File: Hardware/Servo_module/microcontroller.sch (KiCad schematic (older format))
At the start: 22 parts, among them K1 CONN_3, K2 CONN_3, K3 CONN_3, K4 CONN_3, K5 CONN_3, K6 CONN_3, K7 CONN_3, K9 CONN_3, P1 CONN_4_JST, SW1 SW_PUSH

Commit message: [HARDWARE][SERVO_MODULE] Schematic
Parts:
- added D10, D11, D4, D5, D6, D7, D8, D9: LED, ~, symbol LED
- added R10, R11, R12, R13, R6, R7, R8, R9: 220, ~, symbol R
- gave numbers to parts that had none: 3
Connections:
- net +3.3V: now also U?.1 (VBAT)
- net GND: now also D10.2 (K), D11.2 (K), D4.2 (K), D5.2 (K), D6.2 (K), D7.2 (K), D8.2 (K), D9.2 (K)
- net NRST: now also U?.7 (NRST)
- net at U?.25 (PB12): now also R6.1
- net at U?.26 (PB13): now also R7.1
- net at U?.27 (PB14): now also R8.1
- net at U?.28 (PB15): now also R9.1
- net at U?.40 (PB4): now also R10.1
- net at U?.41 (PB5): now also R11.1
- net at U?.42 (PB6): now also R12.1
- net at U?.43 (PB7): now also R13.1
- new net: D4.1 (A), R6.2
- new net: D5.1 (A), R7.2
- new net: D6.1 (A), R8.2
- new net: D7.1 (A), R9.2
- new net: D8.1 (A), R10.2
- new net: D9.1 (A), R11.2
- new net: D10.1 (A), R12.2
- new net: D11.1 (A), R13.2
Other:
- note added: "TEST_LED"

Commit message: [HARDWARE][SERVO_MODULE] Schematic
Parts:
- C7, C8: value C -> 20p
- gave numbers to parts that had none: 1
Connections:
- net USART_PROG_RX: now also U1.31 (PA10)
- net USART_PROG_TX: now also U1.30 (PA9)

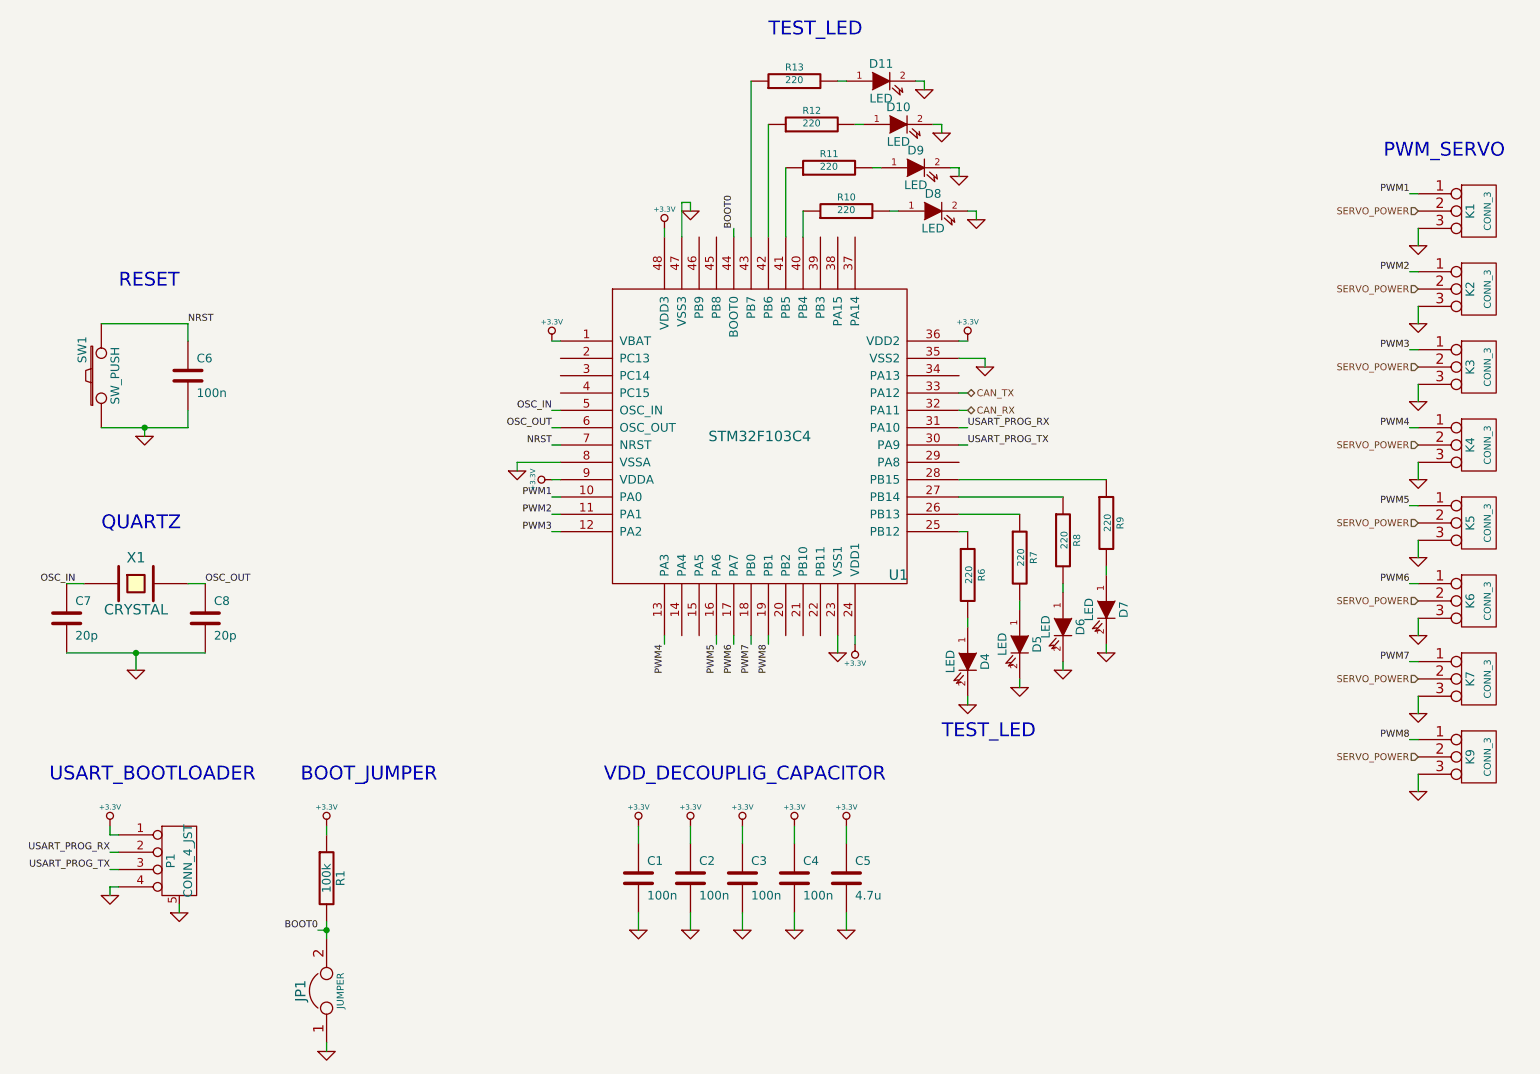
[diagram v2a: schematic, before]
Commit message: [HARDWARE][SERVO_MODULE] Update schemating & routing
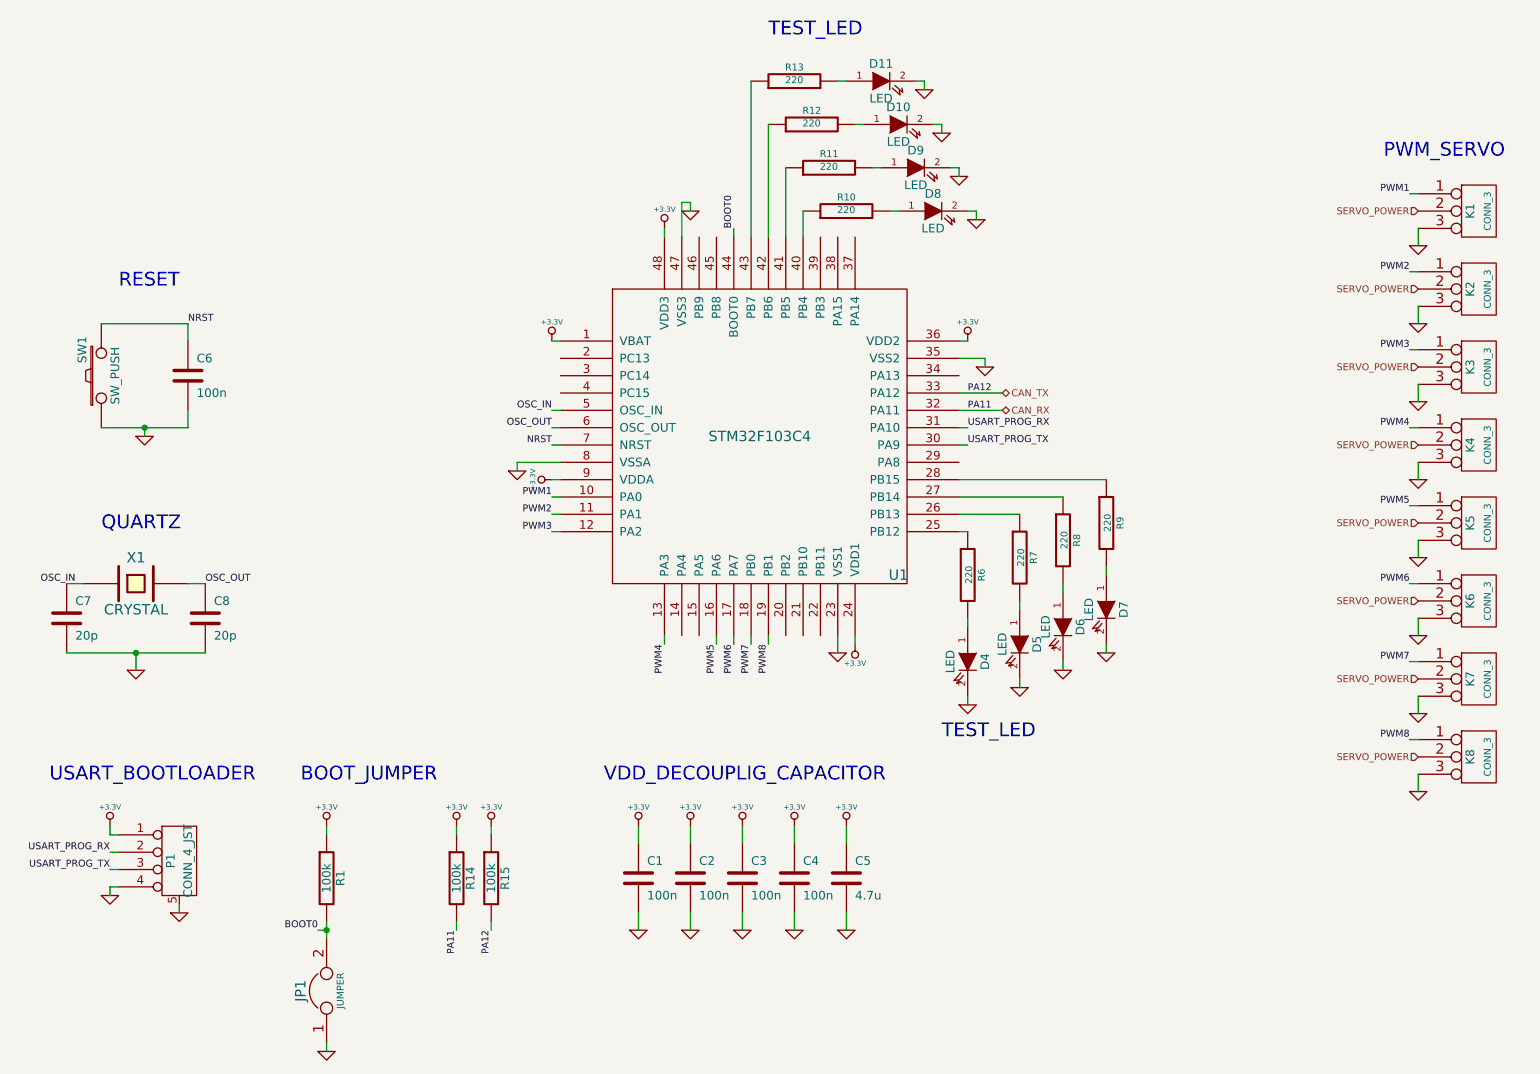
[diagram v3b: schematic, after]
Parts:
- added R14, R15: 100k, symbol R
- renumbered K9 to K8
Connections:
- net +3.3V: now also R14.1, R15.1
- net CAN_RX: now also R14.2
- net CAN_TX: now also R15.2

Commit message: [HARDWARE][SERVO_MOTEUR] Schematic and routing fixes
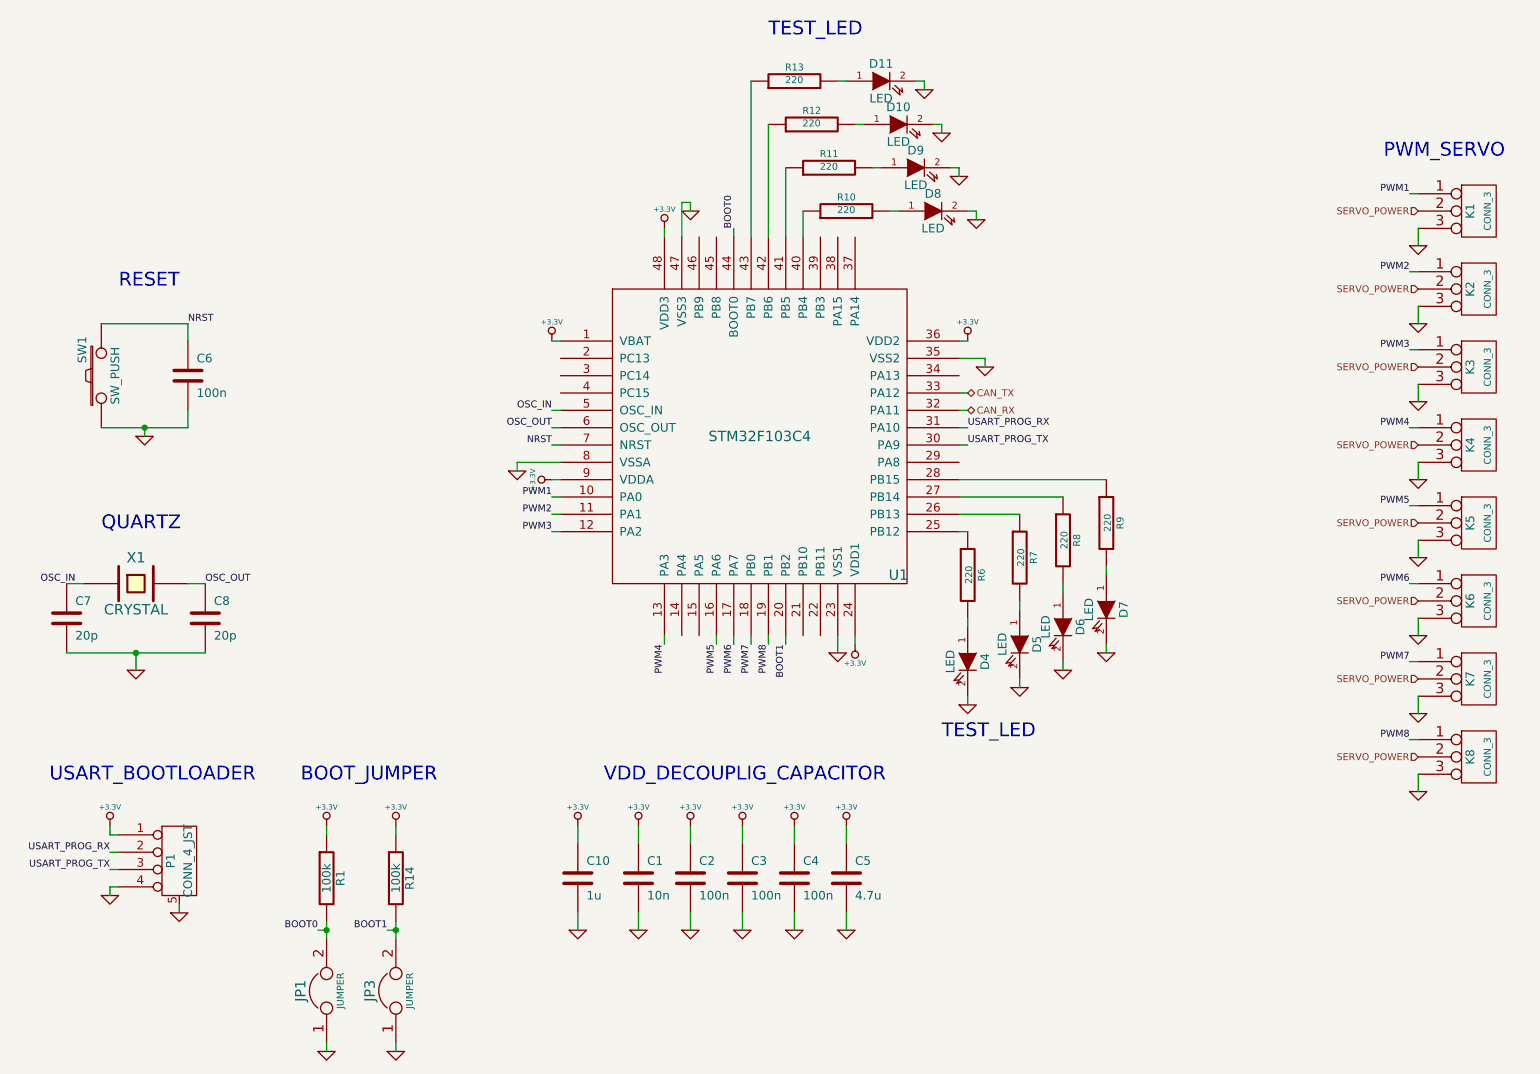
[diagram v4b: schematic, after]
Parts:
- removed R15: 100k, symbol R
- added C10: 1u, symbol C
- added JP3: JUMPER, symbol JUMPER
- C1: value 100n -> 10n
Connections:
- net +3.3V: now also C10.1
- net CAN_RX: no longer R14.2
- net GND: now also C10.2, JP3.1
- net BOOT1: now reaches U1.20 (PB2)
- net BOOT1: now also R14.2, JP3.2
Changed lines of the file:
@@
 Sheet 3 4
 Title ""
-Date "25 oct 2013"
+Date "27 oct 2013"
 Rev ""
 Comp ""
@@
 F 3 "" H 3350 6050 60  0001 C CNN
 	1    3350 6050
-	1    0    0    -1
-$EndComp
-$Comp
-L STM32F103C4 U1
-U 1 1 52611ACD
-P 7250 5500
-F 0 "U1" H 6650 6400 60  0000 C CNN
-F 1 "STM32F103C4" H 5850 7200 60  0000 C CNN
-F 2 "" H 7250 5500 60  0001 C CNN
-F 3 "" H 7250 5500 60  0001 C CNN
-	1    7250 5500
 	1    0    0    -1
 $EndComp
@@
 	1    0    0    -1
 $EndComp
-Text HLabel 7250 3650 2    40   BiDi ~ 0
+Text HLabel 7050 3650 2    40   BiDi ~ 0
 CAN_RX
-Text HLabel 7250 3550 2    40   BiDi ~ 0
+Text HLabel 7050 3550 2    40   BiDi ~ 0
 CAN_TX
 Text Notes 4950 5800 0    80   ~ 0
@@
 P 5150 6350
 F 0 "C1" H 5200 6450 50  0000 L CNN
-F 1 "100n" H 5200 6250 50  0000 L CNN
+F 1 "10n" H 5200 6250 50  0000 L CNN
 F 2 "" H 5150 6350 60  0001 C CNN
 F 3 "" H 5150 6350 60  0001 C CNN
@@
 	9650 3600 9650 3500
 Wire Wire Line
-	7000 3650 7250 3650
-Wire Wire Line
 	5450 6550 5450 6650
 Wire Wire Line
@@
 Wire Wire Line
 	6350 6550 6350 6650
-Wire Wire Line
-	7000 3550 7250 3550
 Wire Wire Line
 	9650 3950 9650 4050
@@
 USART_PROG_TX
 $Comp
+L STM32F103C4 U1
+U 1 1 52611ACD
+P 7250 5500
+F 0 "U1" H 6650 6400 60  0000 C CNN
+F 1 "STM32F103C4" H 5850 7200 60  0000 C CNN
+F 2 "" H 7250 5500 60  0001 C CNN
+F 3 "" H 7250 5500 60  0001 C CNN
+	1    7250 5500
+	1    0    0    -1
+$EndComp
+Wire Wire Line
+	7000 3550 7050 3550
+Wire Wire Line
+	7000 3650 7050 3650
+$Comp
+L +3.3V #PWR048
+U 1 1 526CFDD0
+P 4800 6050
+F 0 "#PWR048" H 4800 6010 30  0001 C CNN
+F 1 "+3.3V" H 4800 6160 30  0000 C CNN
+F 2 "" H 4800 6050 60  0001 C CNN
+F 3 "" H 4800 6050 60  0001 C CNN
+	1    4800 6050
+	1    0    0    -1
+$EndComp
+$Comp
+L GND #PWR049
+U 1 1 526CFDD6
+P 4800 6650
+F 0 "#PWR049" H 4800 6650 30  0001 C CNN
+F 1 "GND" H 4800 6580 30  0001 C CNN
+F 2 "" H 4800 6650 60  0001 C CNN
+F 3 "" H 4800 6650 60  0001 C CNN
+	1    4800 6650
+	1    0    0    -1
+$EndComp
+$Comp
+L C C10
+U 1 1 526CFDEE
+P 4800 6350
+F 0 "C10" H 4850 6450 50  0000 L CNN
+F 1 "1u" H 4850 6250 50  0000 L CNN
+F 2 "" H 4800 6350 60  0001 C CNN
+F 3 "" H 4800 6350 60  0001 C CNN
+	1    4800 6350
+	1    0    0    -1
+$EndComp
+Wire Wire Line
+	4800 6550 4800 6650
+Wire Wire Line
+	4800 6050 4800 6150
+$Comp
+L +3.3V #PWR050
+U 1 1 526CFFD2
+P 3750 6050
+F 0 "#PWR050" H 3750 6010 30  0001 C CNN
+F 1 "+3.3V" H 3750 6160 30  0000 C CNN
+F 2 "" H 3750 6050 60  0001 C CNN
+F 3 "" H 3750 6050 60  0001 C CNN
+	1    3750 6050
+	1    0    0    -1
+$EndComp
+Text Label 3700 6650 2    40   ~ 0
+BOOT1
+$Comp
+L JUMPER JP3
+U 1 1 526CFFD9
+P 3750 7000
+F 0 "JP3" H 3750 7150 60  0000 C CNN
+F 1 "JUMPER" H 3750 6920 40  0000 C CNN
+F 2 "" H 3750 7000 60  0001 C CNN
+F 3 "" H 3750 7000 60  0001 C CNN
+	1    3750 7000
+	0    -1   -1   0
+$EndComp
+$Comp
+L GND #PWR051
+U 1 1 526CFFDF
+P 3750 7350
+F 0 "#PWR051" H 3750 7350 30  0001 C CNN
+F 1 "GND" H 3750 7280 30  0001 C CNN
+F 2 "" H 3750 7350 60  0001 C CNN
+F 3 "" H 3750 7350 60  0001 C CNN
+	1    3750 7350
+	1    0    0    -1
+$EndComp
+$Comp
 L R R14
-U 1 1 526AABD8
-P 4100 6350
-F 0 "R14" V 4180 6350 50  0000 C CNN
-F 1 "100k" V 4100 6350 50  0000 C CNN
-F 2 "" H 4100 6350 60  0001 C CNN
-F 3 "" H 4100 6350 60  0001 C CNN
-	1    4100 6350
-	1    0    0    -1
-$EndComp
-$Comp
-L R R15
-U 1 1 526AABE4
-P 4300 6350
-F 0 "R15" V 4380 6350 50  0000 C CNN
-F 1 "100k" V 4300 6350 50  0000 C CNN
-F 2 "" H 4300 6350 60  0001 C CNN
-F 3 "" H 4300 6350 60  0001 C CNN
-	1    4300 6350
-	1    0    0    -1
-$EndComp
-$Comp
-L +3.3V #PWR048
-U 1 1 526AAC1B
-P 4100 6050
-F 0 "#PWR048" H 4100 6010 30  0001 C CNN
-F 1 "+3.3V" H 4100 6160 30  0000 C CNN
-F 2 "" H 4100 6050 60  0001 C CNN
-F 3 "" H 4100 6050 60  0001 C CNN
-	1    4100 6050
-	1    0    0    -1
-$EndComp
-$Comp
-L +3.3V #PWR049
-U 1 1 526AAC21
-P 4300 6050
-F 0 "#PWR049" H 4300 6010 30  0001 C CNN
-F 1 "+3.3V" H 4300 6160 30  0000 C CNN
-F 2 "" H 4300 6050 60  0001 C CNN
-F 3 "" H 4300 6050 60  0001 C CNN
-	1    4300 6050
-	1    0    0    -1
-$EndComp
-Wire Wire Line
-	4100 6050 4100 6100
-Wire Wire Line
-	4300 6050 4300 6100
-Wire Wire Line
-	4100 6600 4100 6650
-Wire Wire Line
-	4300 6600 4300 6650
-Text Label 4100 6650 3    39   ~ 0
-PA11
-Text Label 4300 6650 3    39   ~ 0
-PA12
-Text Label 7050 3550 0    39   ~ 0
-PA12
-Text Label 7050 3650 0    39   ~ 0
-PA11
+U 1 1 526CFFE5
+P 3750 6350
+F 0 "R14" V 3830 6350 50  0000 C CNN
+F 1 "100k" V 3750 6350 50  0000 C CNN
+F 2 "" H 3750 6350 60  0001 C CNN
+F 3 "" H 3750 6350 60  0001 C CNN
+	1    3750 6350
+	1    0    0    -1
+$EndComp
+Wire Wire Line
+	3750 6050 3750 6100
+Wire Wire Line
+	3750 7300 3750 7350
+Wire Wire Line
+	3750 6600 3750 6700
+Wire Wire Line
+	3750 6650 3700 6650
+Connection ~ 3750 6650
+Wire Wire Line
+	6000 4950 6000 5000
+Text Label 6000 5000 3    40   ~ 0
+BOOT1
 $EndSCHEMATC
